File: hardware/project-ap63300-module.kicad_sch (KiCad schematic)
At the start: 14 parts, among them J1 Conn_01x02_Male, J2 Conn_01x02_Male, J3 Conn_01x02_Male, U1 AP63300WU-7

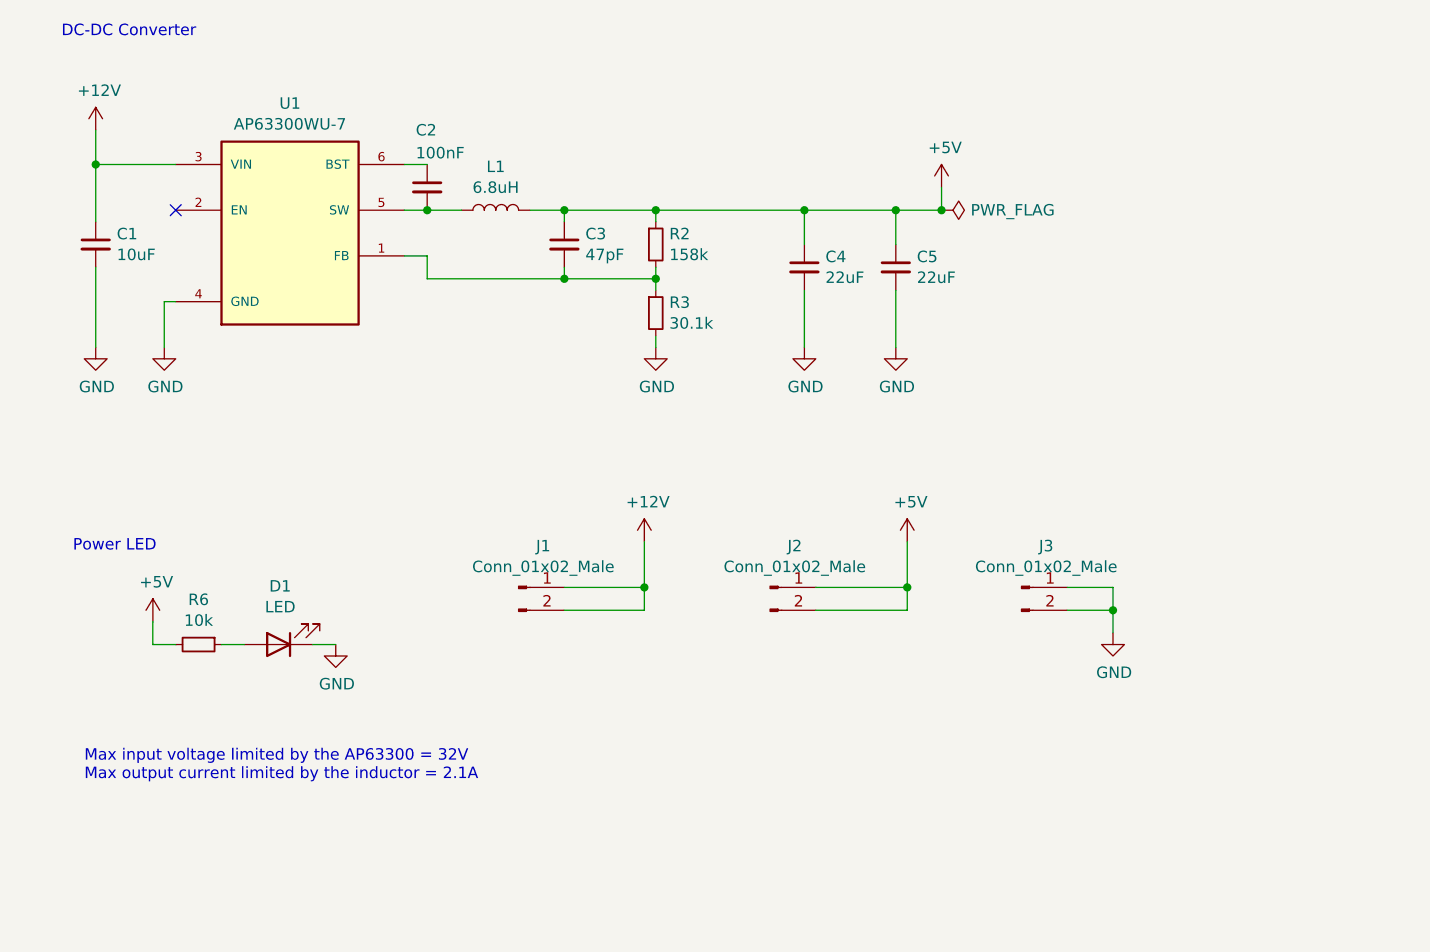
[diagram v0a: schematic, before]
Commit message: Make AP63300 schematic variable
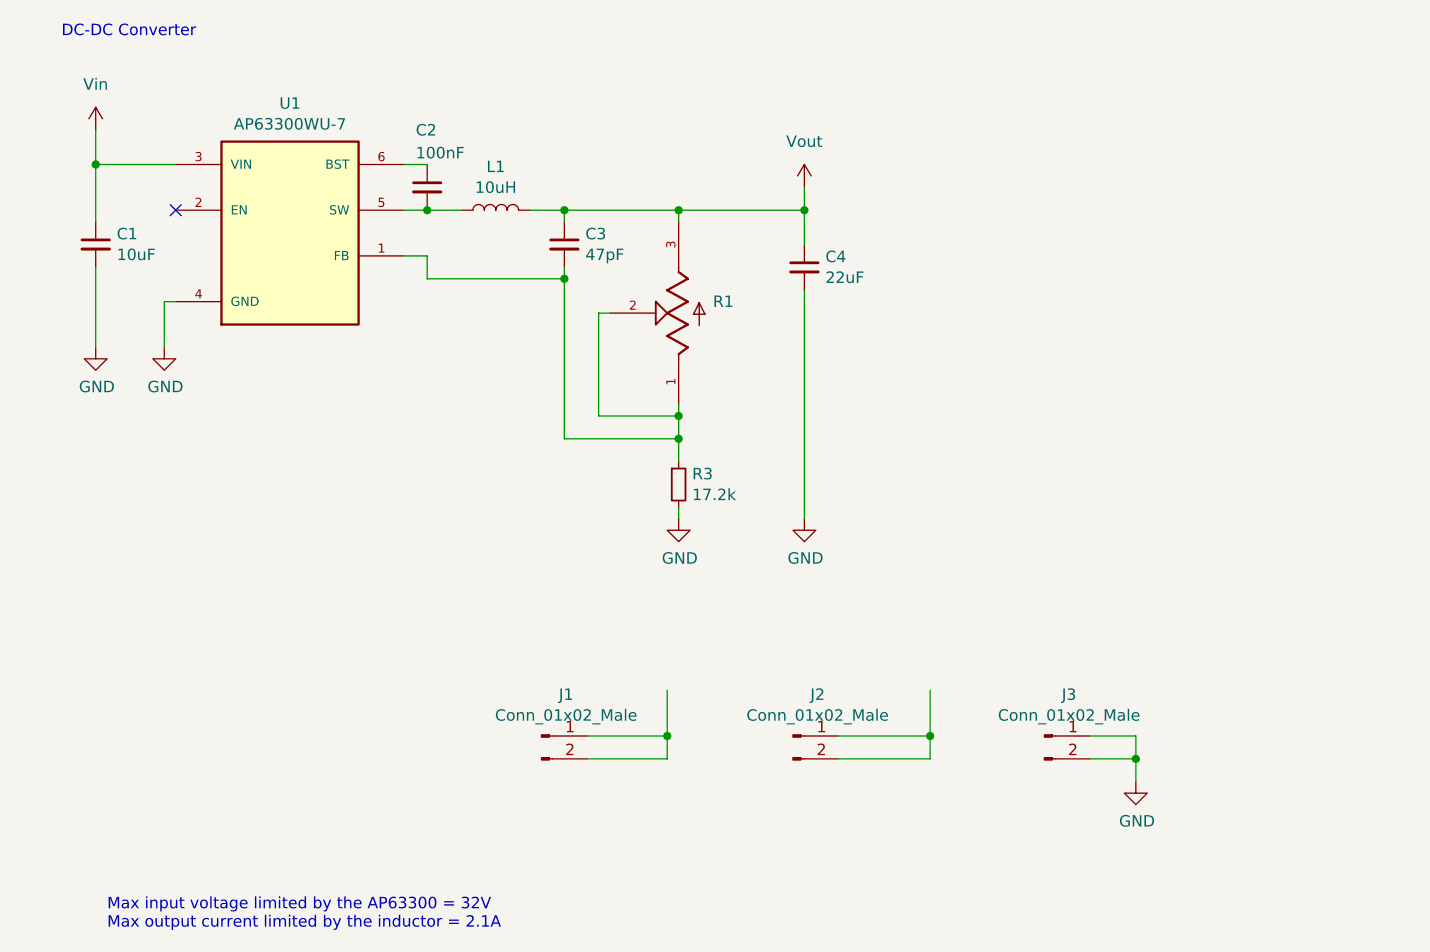
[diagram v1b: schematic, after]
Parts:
- removed C5: 22uF, Capacitor_SMD:C_1210_3225Metric_Pad1.33x2.70mm_HandSolder, symbol Device:C_Small
- removed D1: LED, LED_SMD:LED_0603_1608Metric, symbol Device:LED
- removed R2: 158k, Resistor_SMD:R_0603_1608Metric, symbol Device:R_Small
- removed R6: 10k, Resistor_SMD:R_0603_1608Metric, symbol Device:R_Small
- added R1: TC33X-2-504E, TC33X-2-504E:TRIM_TC33X-2-504E, symbol TC33X-2-504E:TC33X-2-504E
- L1: value 6.8uH -> 10uH; footprint SRP4020TA-6R8M:IND_SRP4020TA-6R8M -> SPM10040T_100M:IND_SPM10040T-100M
- R3: value 30.1k -> 17.2k
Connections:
- net at C3.2, R3.1, U1.1 (FB): now also R1.1, R1.2
- net +12V: no longer names the net of J1.1 (Pin_1), J1.2 (Pin_2)
- net +12V: no longer C1.1, U1.3 (VIN)
- net +5V renamed Vout
- net Vout: now also R1.3; no longer J2.1 (Pin_1), J2.2 (Pin_2)
- new net: J2.1 (Pin_1), J2.2 (Pin_2)
- new net Vin: C1.1, U1.3 (VIN)
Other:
- note removed: "Power LED"
- moved on the sheet: J1, J2, J3, R3

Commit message: sch: add mounting holes
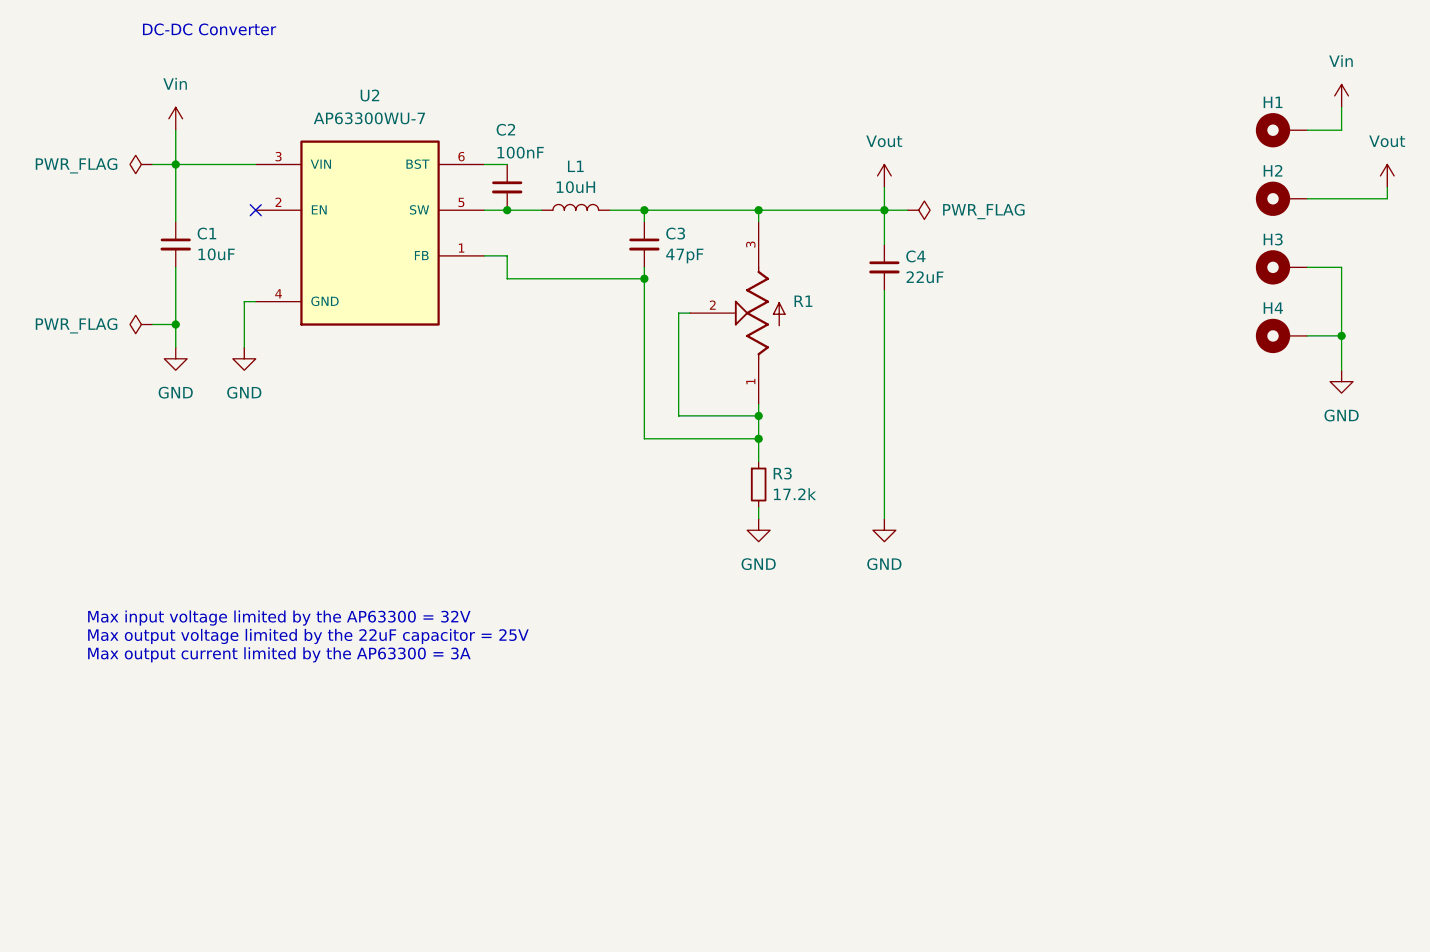
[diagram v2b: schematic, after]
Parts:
- removed J1, J2, J3: Conn_01x02_Male, Connector_PinHeader_2.54mm:PinHeader_1x02_P2.54mm_Vertical, symbol Connector:Conn_01x02_Male
- removed U1: AP63300WU-7, SOT95P280X100-6N, symbol AP63300WU-7:AP63300WU-7
- added H1, H2, H3, H4: MountingHole_Pad, MountingHole:MountingHole_2.2mm_M2_ISO14580_Pad, symbol Mechanical:MountingHole_Pad
- added U2: AP63300WU-7, AP63300WU-7:SOT95P280X100-6N, symbol AP63300WU-7:AP63300WU-7
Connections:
- net GND: now also H3.1, H4.1, U2.4 (GND)
- net Vin: now also H1.1, U2.3 (VIN)
- net Vout: now also H2.1
- net at C3.2, R1.1, R1.2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: now also U2.1 (FB)
- net at C2.2, L1.1: now also U2.5 (SW)
- net at C2.1: now also U2.6 (BST)
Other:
- note added: "Max input voltage limited by the AP63300 = 32V Max output voltage limited by the 22uF capacitor = 25V Max output current limited by the AP63300 = 3A"
- note removed: "Max input voltage limited by the AP63300 = 32V Max output current limited by the inductor = 2.1A"
- moved on the sheet: C1, C2, C3, C4, L1, R1, R3

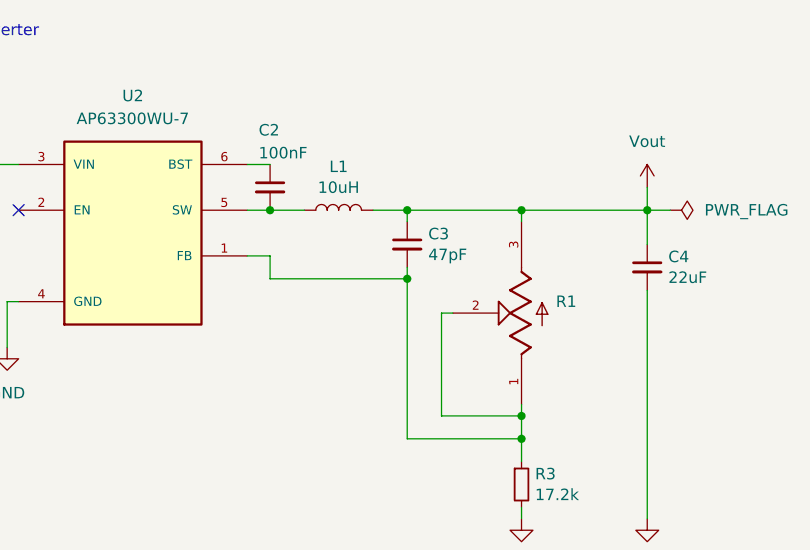
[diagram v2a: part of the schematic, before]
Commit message: pcb: first placement
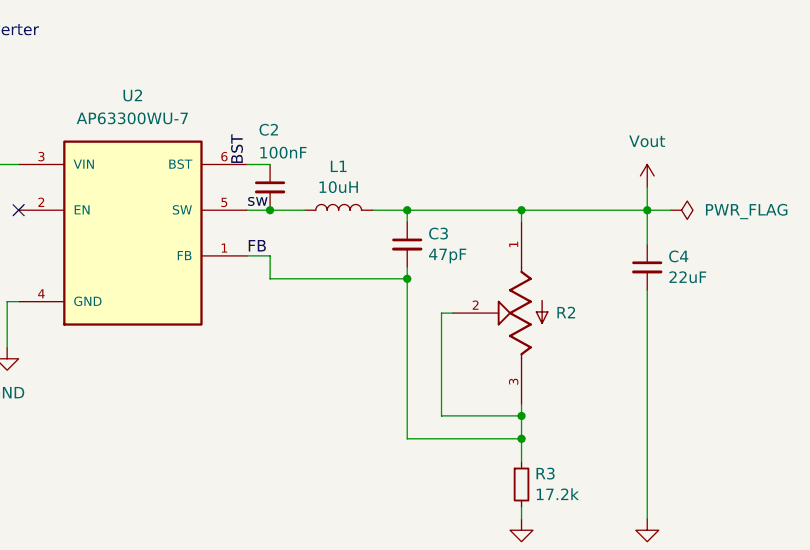
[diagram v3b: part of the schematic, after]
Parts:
- removed R1: TC33X-2-504E, TC33X-2-504E:TRIM_TC33X-2-504E, symbol TC33X-2-504E:TC33X-2-504E
- added R2: TC33X-2-504E, TC33X_2_504E:TRIM_TC33X-2-504E, symbol TC33X-2-504E:TC33X-2-504E
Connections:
- net Vout: now also R2.1
- net FB: now reaches C3.2, R3.1, U2.1 (FB)
- net FB: now also R2.2, R2.3
- net BST: now reaches C2.1, U2.6 (BST)
- net sw: now reaches C2.2, L1.1, U2.5 (SW)
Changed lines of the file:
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@@
+		)
+	)
+	(label "sw"
+		(at 67.31 38.1 0)
+		(fields_autoplaced yes)
+		(effects
+			(font
+				(size 1.27 1.27)
+			)
+			(justify left bottom)
+		)
+	)
+	(label "BST"
+		(at 67.31 33.02 90)
+		(fields_autoplaced yes)
+		(effects
+			(font
+				(size 1.27 1.27)
+			)
+			(justify left bottom)
+		)
+	)
+	(label "FB"
+		(at 67.31 43.18 0)
+		(fields_autoplaced yes)
+		(effects
+			(font
+				(size 1.27 1.27)
+			)
+			(justify left bottom)
 		)
 	)
@@
 	)
 	(symbol
-		(lib_id "TC33X-2-504E:TC33X-2-504E")
-		(at 97.79 49.53 90)
-		(unit 1)
-		(exclude_from_sim no)
-		(in_bom yes)
-		(on_board yes)
-		(dnp no)
-		(property "Reference" "R1"
-			(at 101.6 48.2599 90)
-			(effects
-				(font
-					(size 1.27 1.27)
-				)
-				(justify right)
-			)
-		)
-		(property "Value" "TC33X-2-504E"
-			(at 101.6 50.7999 90)
-			(effects
-				(font
-					(size 1.27 1.27)
-				)
-				(justify right)
-				(hide yes)
-			)
-		)
-		(property "Footprint" "TC33X-2-504E:TRIM_TC33X-2-504E"
-			(at 97.79 49.53 0)
-			(effects
-				(font
-					(size 1.27 1.27)
-				)
-				(justify bottom)
-				(hide yes)
-			)
-		)
-		(property "Datasheet" ""
-			(at 97.79 49.53 0)
-			(effects
-				(font
-					(size 1.27 1.27)
-				)
-				(hide yes)
-			)
-		)
-		(property "Description" ""
-			(at 97.79 49.53 0)
-			(effects
-				(font
-					(size 1.27 1.27)
-				)
-				(hide yes)
-			)
-		)
-		(property "MF" "Bourns"
-			(at 97.79 49.53 0)
-			(effects
-				(font
-					(size 1.27 1.27)
-				)
-				(justify bottom)
-				(hide yes)
-			)
-		)
-		(property "DESCRIPTION" "Res Trimmer 100K Ohm 25% 1/10W 1_Elec_/1_Mech_Turn _3 X 3.8mm_ Foot Print SMD Embossed T/R"
-			(at 97.79 49.53 0)
-			(effects
-				(font
-					(size 1.27 1.27)
-				)
-				(justify bottom)
-				(hide yes)
-			)
-		)
-		(property "PACKAGE" "Bourns"
-			(at 97.79 49.53 0)
-			(effects
-				(font
-					(size 1.27 1.27)
-				)
-				(justify bottom)
-				(hide yes)
-			)
-		)
-		(property "PRICE" "None"
-			(at 97.79 49.53 0)
-			(effects
-				(font
-					(size 1.27 1.27)
-				)
-				(justify bottom)
-				(hide yes)
-			)
-		)
-		(property "MP" "TC33X-2-104E"
-			(at 97.79 49.53 0)
-			(effects
-				(font
-					(size 1.27 1.27)
-				)
-				(justify bottom)
-				(hide yes)
-			)
-		)
-		(property "AVAILABILITY" "Unavailable"
-			(at 97.79 49.53 0)
-			(effects
-				(font
-					(size 1.27 1.27)
-				)
-				(justify bottom)
-				(hide yes)
-			)
-		)
-		(pin "1"
-		)
-		(pin "3"
-		)
-		(pin "2"
-		)
-		(instances
-			(project ""
-				(path "/4d25b0a3-aea0-4711-9e74-24157a752b25"
-					(reference "R1")
-					(unit 1)
-				)
-			)
-		)
-	)
-	(symbol
 		(lib_id "power:GND")
 		(at 162.56 55.88 0)
@@
 					(unit 1)
 				)
+			)
+		)
+	)
+	(symbol
+		(lib_name "TC33X-2-504E_1")
+		(lib_id "TC33X-2-504E:TC33X-2-504E")
+		(at 97.79 49.53 90)
+		(mirror x)
+		(unit 1)
+		(exclude_from_sim no)
+		(in_bom yes)
+		(on_board yes)
+		(dnp no)
+		(property "Reference" "R2"
+			(at 101.6 49.5301 90)
+			(effects
+				(font
+					(size 1.27 1.27)
+				)
+				(justify right)
+			)
+		)
+		(property "Value" "TC33X-2-504E"
+			(at 101.6 48.2601 90)
+			(effects
+				(font
+					(size 1.27 1.27)
+				)
+				(justify right)
+				(hide yes)
+			)
+		)
+		(property "Footprint" "TC33X_2_504E:TRIM_TC33X-2-504E"
+			(at 97.79 49.53 0)
+			(effects
+				(font
+					(size 1.27 1.27)
+				)
+				(justify bottom)
+				(hide yes)
+			)
+		)
+		(property "Datasheet" ""
+			(at 97.79 49.53 0)
+			(effects
+				(font
+					(size 1.27 1.27)
+				)
+				(hide yes)
+			)
+		)
+		(property "Description" "Res Trimmer 100K Ohm 25% 1/10W 1_Elec_/1_Mech_Turn _3 X 3.8mm_ Foot Print SMD Embossed T/R"
+			(at 97.79 49.53 0)
+			(effects
+				(font
+					(size 1.27 1.27)
+				)
+				(justify bottom)
+				(hide yes)
+			)
+		)
+		(property "MF" "Bourns"
+			(at 97.79 49.53 0)
+			(effects
+				(font
+					(size 1.27 1.27)
+				)
+				(justify bottom)
+				(hide yes)
+			)
+		)
+		(property "PACKAGE" "Bourns"
+			(at 97.79 49.53 0)
+			(effects
+				(font
+					(size 1.27 1.27)
+				)
+				(justify bottom)
+				(hide yes)
+			)
+		)
+		(property "PRICE" "None"
+			(at 97.79 49.53 0)
+			(effects
+				(font
+					(size 1.27 1.27)
+				)
+				(justify bottom)
+				(hide yes)
+			)
+		)
+		(property "MP" "TC33X-2-104E"
+			(at 97.79 49.53 0)
+			(effects
+				(font
+					(size 1.27 1.27)
+				)
+				(justify bottom)
+				(hide yes)
+			)
+		)
+		(property "AVAILABILITY" "Unavailable"
+			(at 97.79 49.53 0)
+			(effects
+				(font
+					(size 1.27 1.27)
+				)
+				(justify bottom)
+				(hide yes)
+			)
+		)
+		(pin "1"
+		)
+		(pin "3"
+		)
+		(pin "2"
+		)
+		(instances
+			(project ""
+				(path "/4d25b0a3-aea0-4711-9e74-24157a752b25"
+					(reference "R2")
+					(unit 1)
+				)

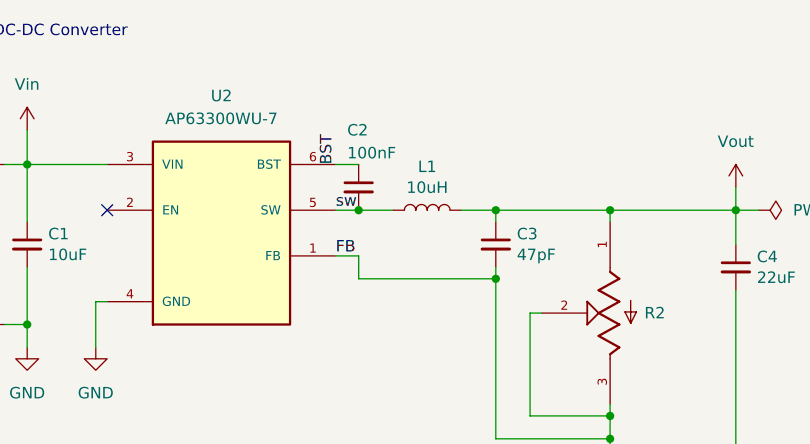
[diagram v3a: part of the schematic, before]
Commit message: pcb: first routing draft
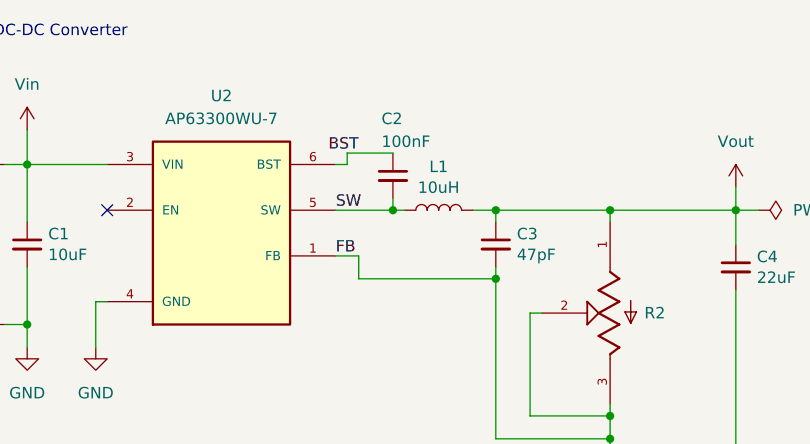
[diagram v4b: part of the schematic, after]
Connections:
- net sw renamed SW
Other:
- moved on the sheet: C2, L1
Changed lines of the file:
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@@
+	)
+	(junction
+		(at 73.66 38.1)
+		(diameter 0)
+		(color 0 0 0 0)
 	)
 	(junction
@@
 	)
 	(junction
-		(at 69.85 38.1)
-		(diameter 0)
-		(color 0 0 0 0)
-	)
-	(junction
 		(at 162.56 52.07)
 		(diameter 0)
@@
 	(wire
 		(pts
-			(xy 81.28 38.1) (xy 85.09 38.1)
+			(xy 82.55 38.1) (xy 85.09 38.1)
 		)
 		(stroke
@@
 	(wire
 		(pts
+			(xy 73.66 38.1) (xy 74.93 38.1)
+		)
+		(stroke
+			(width 0)
+			(type default)
+		)
+	)
+	(wire
+		(pts
 			(xy 85.09 63.5) (xy 97.79 63.5)
 		)
@@
 	(wire
 		(pts
-			(xy 69.85 38.1) (xy 67.31 38.1)
+			(xy 67.31 38.1) (xy 73.66 38.1)
 		)
 		(stroke
@@
 	(wire
 		(pts
+			(xy 68.58 31.75) (xy 68.58 33.02)
+		)
+		(stroke
+			(width 0)
+			(type default)
+		)
+	)
+	(wire
+		(pts
+			(xy 73.66 36.83) (xy 73.66 38.1)
+		)
+		(stroke
+			(width 0)
+			(type default)
+		)
+	)
+	(wire
+		(pts
 			(xy 85.09 38.1) (xy 97.79 38.1)
 		)
@@
 	(wire
 		(pts
+			(xy 68.58 31.75) (xy 73.66 31.75)
+		)
+		(stroke
+			(width 0)
+			(type default)
+		)
+	)
+	(wire
+		(pts
 			(xy 162.56 52.07) (xy 162.56 55.88)
 		)
@@
 	(wire
 		(pts
+			(xy 68.58 33.02) (xy 67.31 33.02)
+		)
+		(stroke
+			(width 0)
+			(type default)
+		)
+	)
+	(wire
+		(pts
 			(xy 158.75 52.07) (xy 162.56 52.07)
 		)
@@
 		(pts
 			(xy 40.64 53.34) (xy 40.64 48.26)
-		)
-		(stroke
-			(width 0)
-			(type default)
-		)
-	)
-	(wire
-		(pts
-			(xy 69.85 38.1) (xy 73.66 38.1)
-		)
-		(stroke
-			(width 0)
-			(type default)
-		)
-	)
-	(wire
-		(pts
-			(xy 67.31 33.02) (xy 69.85 33.02)
 		)
 		(stroke
@@
 		)
 	)
-	(label "sw"
+	(label "SW"
 		(at 67.31 38.1 0)
 		(fields_autoplaced yes)
@@
 	)
 	(label "BST"
-		(at 67.31 33.02 90)
+		(at 69.85 31.75 180)
 		(fields_autoplaced yes)
 		(effects
@@
 				(size 1.27 1.27)
 			)
-			(justify left bottom)
+			(justify right bottom)
 		)
 	)
@@
 	(symbol
 		(lib_id "Device:C_Small")
-		(at 69.85 35.56 0)
+		(at 73.66 34.29 0)
 		(unit 1)
 		(exclude_from_sim no)
@@
 		(dnp no)
 		(property "Reference" "C2"
-			(at 68.58 29.21 0)
+			(at 72.39 27.94 0)
 			(effects
 				(font
@@
 		)
 		(property "Value" "100nF"
-			(at 68.58 31.75 0)
+			(at 72.39 30.48 0)
 			(effects
 				(font
@@
 		)
 		(property "Footprint" "Capacitor_SMD:C_0603_1608Metric"
-			(at 69.85 35.56 0)
+			(at 73.66 34.29 0)
 			(effects
 				(font
@@
 		)
 		(property "Datasheet" "~"
-			(at 69.85 35.56 0)
+			(at 73.66 34.29 0)
 			(effects
 				(font
@@
 		)
 		(property "Description" ""
-			(at 69.85 35.56 0)
+			(at 73.66 34.29 0)
 			(effects
 				(font
@@
 	(symbol
 		(lib_id "Device:L")
-		(at 77.47 38.1 90)
+		(at 78.74 38.1 90)
 		(unit 1)
 		(exclude_from_sim no)
@@
 		(dnp no)
 		(property "Reference" "L1"
-			(at 77.47 33.274 90)
+			(at 78.74 33.274 90)
 			(effects
 				(font
@@
 		)
 		(property "Value" "10uH"
-			(at 77.47 35.5854 90)
+			(at 78.74 35.5854 90)
 			(effects
 				(font
@@
 		)
 		(property "Footprint" "SPM10040T_100M:IND_SPM10040T-100M"
-			(at 77.47 38.1 0)
+			(at 78.74 38.1 0)
 			(effects
 				(font
@@
 		)
 		(property "Datasheet" "~"
-			(at 77.47 38.1 0)
+			(at 78.74 38.1 0)
 			(effects
 				(font
@@
 		)
 		(property "Description" ""
-			(at 77.47 38.1 0)
-			(effects
-				(font
+			(at 78.74 38.1 0)
+			(effects
+				(font
